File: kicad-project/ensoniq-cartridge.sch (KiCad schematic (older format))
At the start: 13 parts, among them J1 Conn_01x04_Male, SW2 TOGGLE_SW_SPST, SW3 TOGGLE_SW_SPST, U1 AT28C64B-15PU, U2 ensoniq-cartridge-edge-connec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

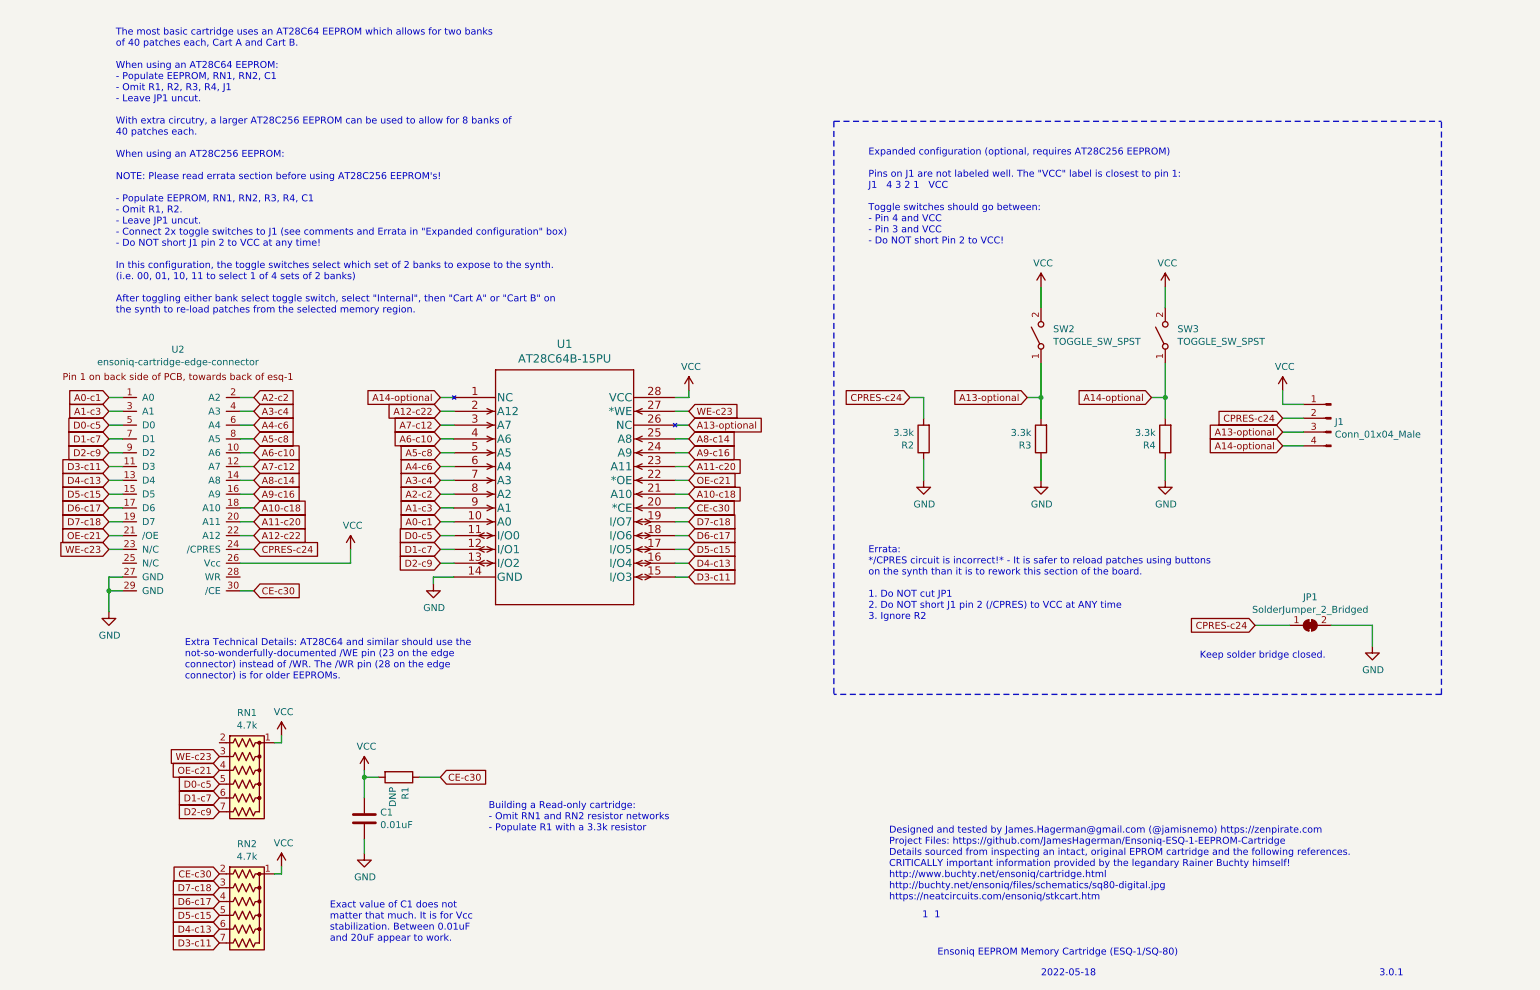
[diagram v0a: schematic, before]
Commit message: Updating schematic with initialization steps and adding schematic image to repo.
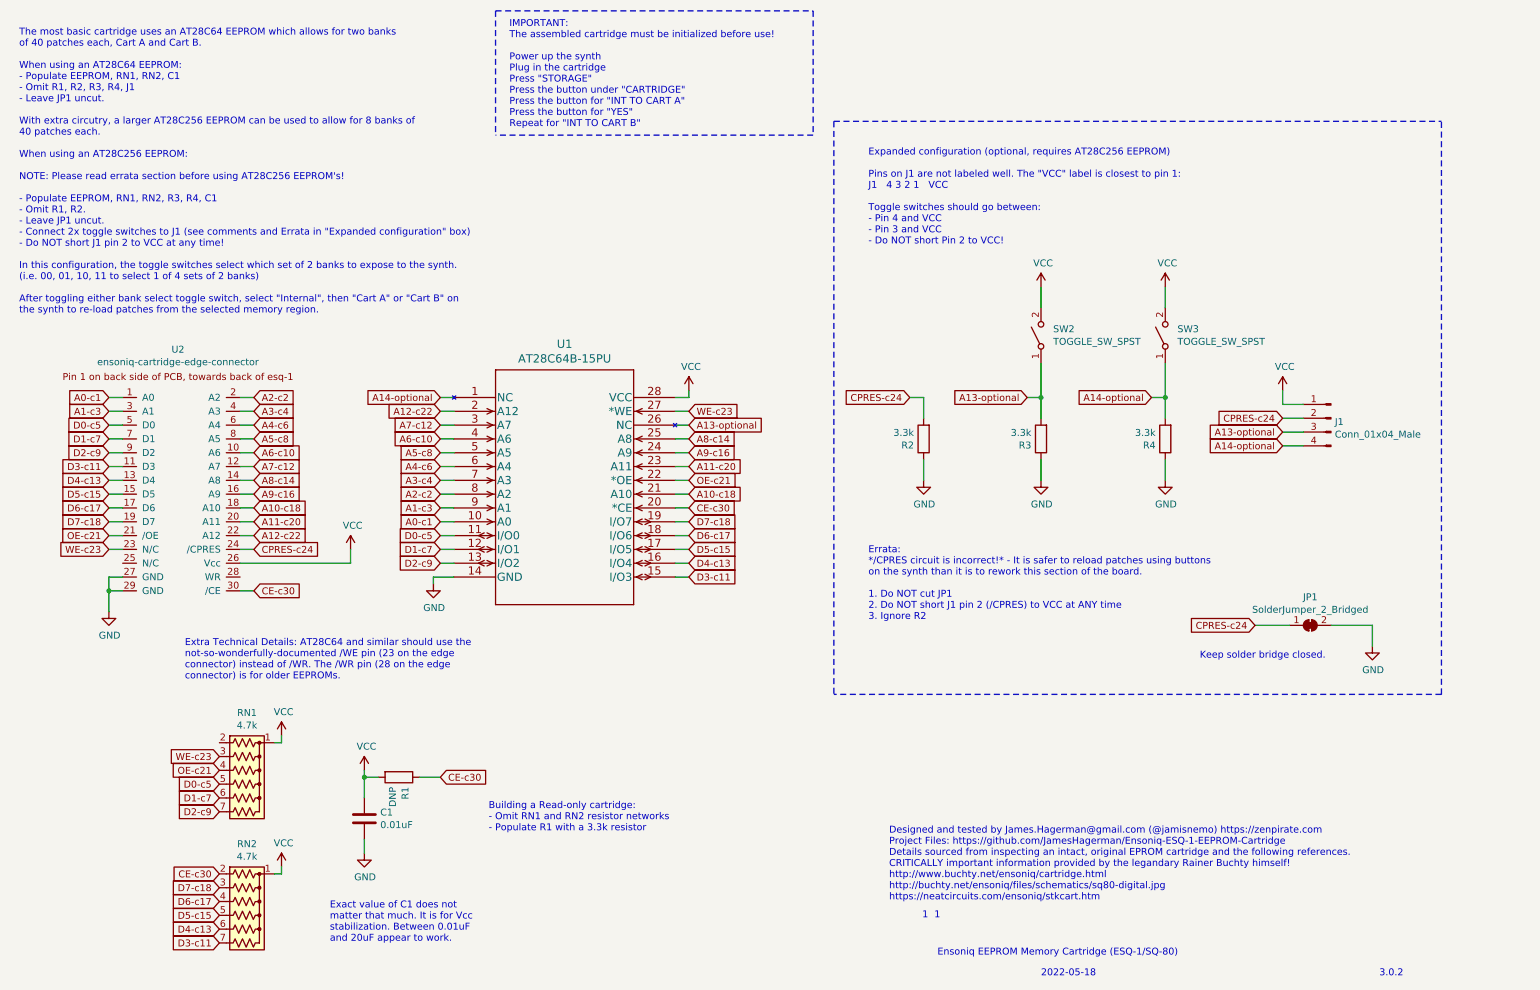
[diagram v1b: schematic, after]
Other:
- note added: "3.0.2"
- note added: "IMPORTANT:\nThe assembled cartridge must be initialized before use!\n\nPower up the synth\nPlug in the cartridge\nPress "STORAGE"\nPress the button under "CARTRIDGE"\nPress the button for "INT TO CART A"\nPress the button for "YES"\nRepeat for "INT TO CART B""
- note removed: "3.0.1"
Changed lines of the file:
@@
 1  1
 Text Notes 10600 7650 0    50   ~ 0
-3.0.1
+3.0.2
 $Comp
 L power:VCC #PWR010
@@
 Text Notes 3000 7400 0    50   ~ 0
 Exact value of C1 does not \nmatter that much. It is for Vcc\nstabilization. Between 0.01uF\nand 20uF appear to work.
-Text Notes 1450 2850 0    50   ~ 0
+Text Notes 750  2850 0    50   ~ 0
 The most basic cartridge uses an AT28C64 EEPROM which allows for two banks\nof 40 patches each, Cart A and Cart B.\n\nWhen using an AT28C64 EEPROM:\n- Populate EEPROM, RN1, RN2, C1\n- Omit R1, R2, R3, R4, J1\n- Leave JP1 uncut.\n\nWith extra circutry, a larger AT28C256 EEPROM can be used to allow for 8 banks of\n40 patches each.\n\nWhen using an AT28C256 EEPROM:\n\nNOTE: Please read errata section before using AT28C256 EEPROM's!\n\n- Populate EEPROM, RN1, RN2, R3, R4, C1\n- Omit R1, R2.\n- Leave JP1 uncut.\n- Connect 2x toggle switches to J1 (see comments and Errata in "Expanded configuration" box)\n- Do NOT short J1 pin 2 to VCC at any time!\n\nIn this configuration, the toggle switches select which set of 2 banks to expose to the synth.\n(i.e. 00, 01, 10, 11 to select 1 of 4 sets of 2 banks) \n\nAfter toggling either bank select toggle switch, select "Internal", then "Cart A" or "Cart B" on\nthe synth to re-load patches from the selected memory region.
 Text Notes 6900 2350 0    50   ~ 0
@@
 Wire Notes Line
 	6650 1450 11050 1450
+Text Notes 4300 1500 0    50   ~ 0
+IMPORTANT:\nThe assembled cartridge must be initialized before use!\n\nPower up the synth\nPlug in the cartridge\nPress "STORAGE"\nPress the button under "CARTRIDGE"\nPress the button for "INT TO CART A"\nPress the button for "YES"\nRepeat for "INT TO CART B"
+Wire Notes Line style solid rgb(255, 0, 0)
+	4200 650  6500 650
+Wire Notes Line style solid rgb(255, 0, 0)
+	6500 1550 4200 1550
+Wire Notes Line style solid rgb(255, 0, 0)
+	6500 650  6500 1550
+Wire Notes Line style solid rgb(255, 0, 0)
+	4200 650  4200 1550
 $EndSCHEMATC

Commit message: Updating schamtic and PDF build instructions to be more human readable.
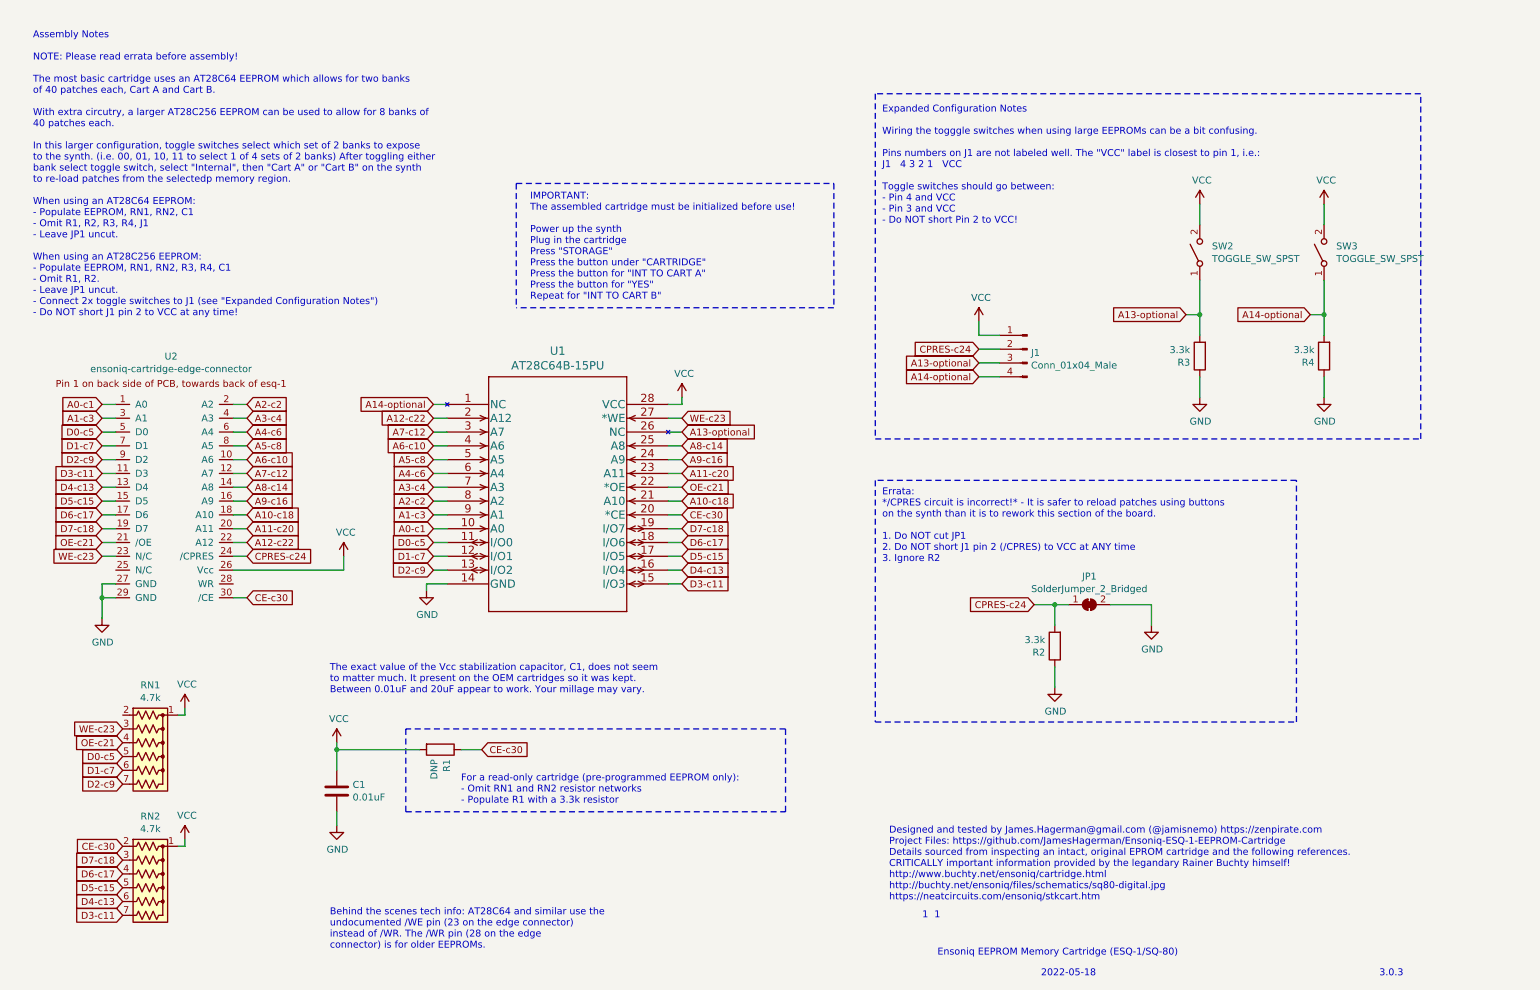
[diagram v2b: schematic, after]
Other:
- note added: "3.0.3"
- note added: "Assembly Notes\n \nNOTE: Please read errata before assembly!\n\nThe most basic cartridge uses an AT28C64 EEPROM which allows for two banks\nof 40 patches each, Cart A and Cart B.\n\nWith extra circutry, a larger AT28C256 EEPROM can be used to allow for 8 banks of\n40 patches each.\n\nIn this larger configuration, toggle switches select which set of 2 banks to expose\nto the synth. (i.e. 00, 01, 1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"
- note added: "Behind the scenes tech info: AT28C64 and similar use the\nundocumented /WE pin (23 on the edge connector)\ninstead of /WR. The /WR pin (28 on the edge\nconnector) is for older EEPROMs."
- note added: "Errata:\n*/CPRES circuit is incorrect!* - It is safer to reload patches using buttons\non the synth than it is to rework this section of the board.\n\n1. Do NOT cut JP1\n2. Do NOT short J1 pin 2 (/CPRES) to VCC at ANY time\n3. Ignore R2"
- note added: "Expanded Configuration Notes\n\nWiring the togggle switches when using large EEPROMs can be a bit confusing.\n\nPins numbers on J1 are not labeled well. The "VCC" label is closest to pin 1, i.e.:\nJ1 4 3 2 1 VCC\n\nToggle switches should go between:\n- Pin 4 and VCC\n- Pin 3 and VCC\n- Do NOT short Pin 2 to VCC!"
- note added: "For a read-only cartridge (pre-programmed EEPROM only):\n- Omit RN1 and RN2 resistor networks\n- Populate R1 with a 3.3k resistor"
- note added: "The exact value of the Vcc stabilization capacitor, C1, does not seem\nto matter much. It present on the OEM cartridges so it was kept.\nBetween 0.01uF and 20uF appear to work. Your millage may vary."
- note removed: "3.0.2"
- note removed: "Building a Read-only cartridge:\n- Omit RN1 and RN2 resistor networks\n- Populate R1 with a 3.3k resistor"
- note removed: "Errata:\n*/CPRES circuit is incorrect!* - It is safer to reload patches using buttons\non the synth than it is to rework this section of the board.\n\n1. Do NOT cut JP1\n2. Do NOT short J1 pin 2 (/CPRES) to VCC at ANY time\n3. Ignore R2\n\n"
- note removed: "Exact value of C1 does not \nmatter that much. It is for Vcc\nstabilization. Between 0.01uF\nand 20uF appear to work."
- note removed: "Expanded configuration (optional, requires AT28C256 EEPROM)\n\nPins on J1 are not labeled well. The "VCC" label is closest to pin 1:\nJ1 4 3 2 1 VCC\n\nToggle switches should go between:\n- Pin 4 and VCC\n- Pin 3 and VCC\n- Do NOT short Pin 2 to VCC!"
- note removed: "Extra Technical Details: AT28C64 and similar should use the\nnot-so-wonderfully-documented /WE pin (23 on the edge\nconnector) instead of /WR. The /WR pin (28 on the edge\nconnector) is for older EEPROMs."
- note removed: "Keep solder bridge closed."
- note removed: "The most basic cartridge uses an AT28C64 EEPROM which allows for two banks\nof 40 patches each, Cart A and Cart B.\n\nWhen using an AT28C64 EEPROM:\n- Populate EEPROM, RN1, RN2, C1\n- Omit R1, R2, R3, R4, J1\n- Leave JP1 uncut.\n\nWith extra circutry, a larger AT28C256 EEPROM can be used to allow for 8 banks of\n40 patches each.\n\nWhen using an AT28C256 EEPROM:\n\nNOTE: Please read errata sectio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"
- moved on the sheet: C1, J1, JP1, R1, R2, R3, R4, RN1, RN2, SW2, SW3, U1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

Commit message: Updating README.me and assembly notes and schematic PDF to include stability suggestions relating to C1.
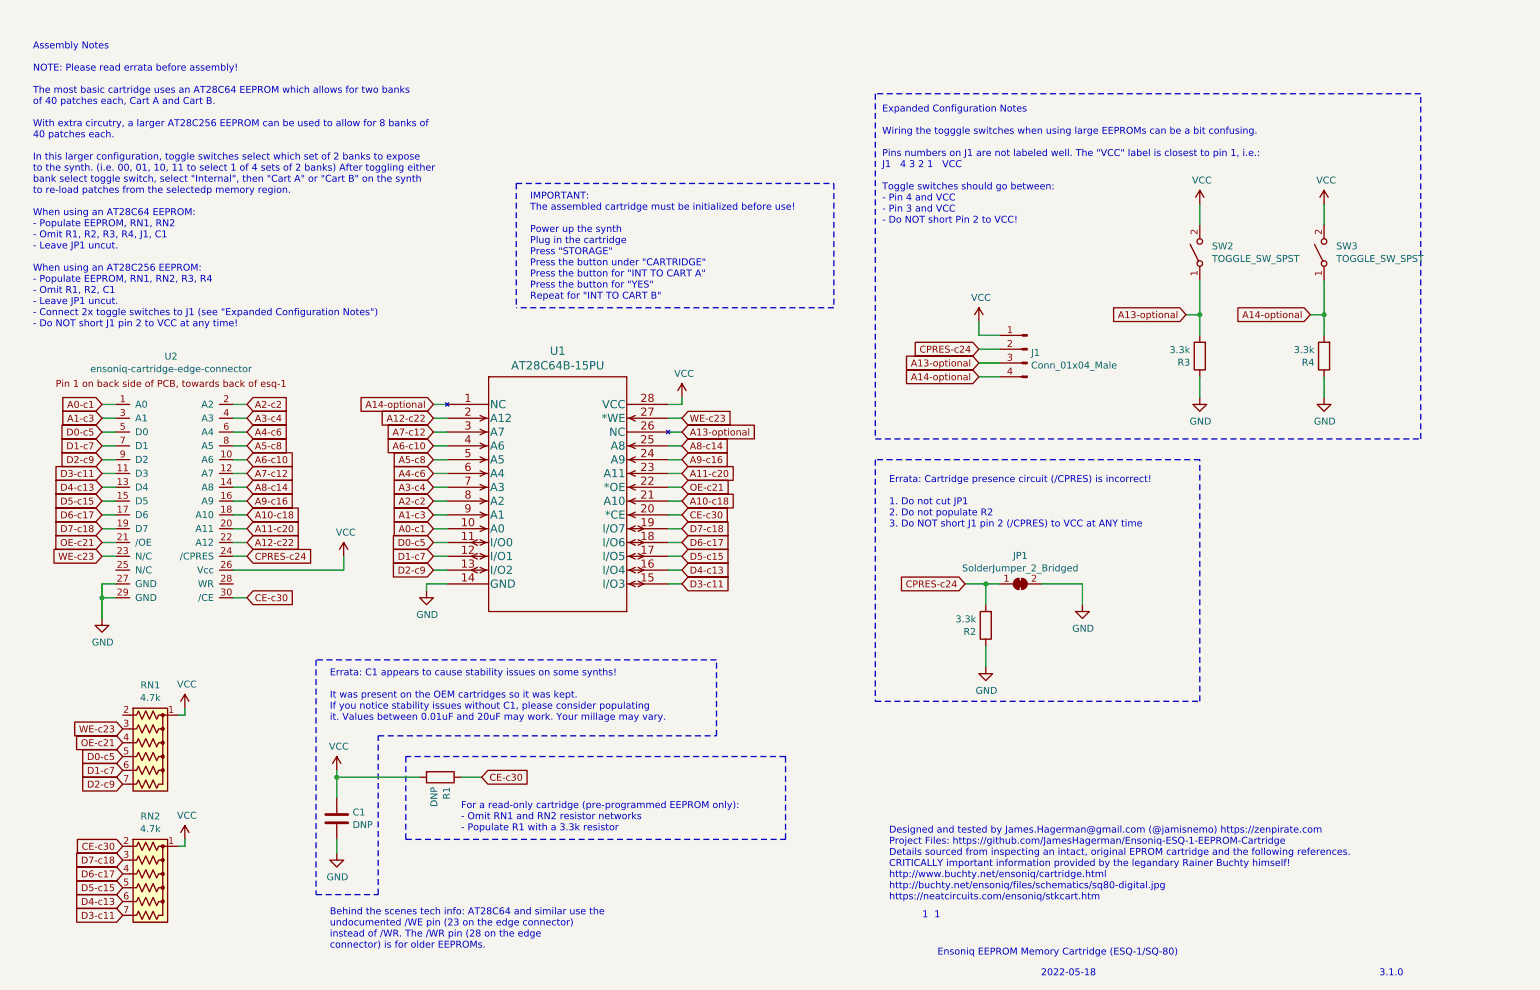
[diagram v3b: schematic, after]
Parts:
- C1: value 0.01uF -> DNP
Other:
- note added: "3.1.0"
- note added: "Errata: C1 appears to cause stability issues on some synths!\n\nIt was present on the OEM cartridges so it was kept.\nIf you notice stability issues without C1, please consider populating\nit. Values between 0.01uF and 20uF may work. Your millage may vary."
- note added: "Errata: Cartridge presence circuit (/CPRES) is incorrect!\n\n1. Do not cut JP1\n2. Do not populate R2\n3. Do NOT short J1 pin 2 (/CPRES) to VCC at ANY time"
- note removed: "3.0.3"
- note removed: "Errata:\n*/CPRES circuit is incorrect!* - It is safer to reload patches using buttons\non the synth than it is to rework this section of the board.\n\n1. Do NOT cut JP1\n2. Do NOT short J1 pin 2 (/CPRES) to VCC at ANY time\n3. Ignore R2"
- note removed: "The exact value of the Vcc stabilization capacitor, C1, does not seem\nto matter much. It present on the OEM cartridges so it was kept.\nBetween 0.01uF and 20uF appear to work. Your millage may vary."
- moved on the sheet: C1, JP1, R1, R2
